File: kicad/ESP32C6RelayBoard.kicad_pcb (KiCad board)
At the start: 2 copper layers, 110.5 x 85.5 mm, 123 parts, among them IC1 SPX1117M3-L-3-3_TR, J1 Screw_Terminal_01x02, J10 Screw_Terminal_01x03, J11 Screw_Terminal_01x03, J12 Screw_Terminal_01x03, J13 Screw_Terminal_01x03, J2 Conn_02x08_Odd_Even, J3 Screw_Terminal_01x02, J4 Screw_Terminal_01x02, J5 10118192-0001LF, J6 Screw_Terminal_01x02, J7 Screw_Terminal_01x02, J8 Screw_Terminal_01x03, J9 Screw_Terminal_01x03, K1 G5RL-K1-E-DC12, K2 G5RL-K1-E-DC12, K3 G5RL-K1-E-DC12, K4 G5RL-K1-E-DC12, Q1 FDN302P, U1 AP62300Z6-7, U10 INA232AIDDFR, U11 74HC237, U12 INA232AIDDFR, U13 FAN3241TMX, U14 FAN3241TMX, U2 ESP32-C6-MINI-1/U, U3 434133025816, U4 434133025816, U5 ESD401DPYR, U6 ESD401DPYR, U7 ESD401DPYR, U8 FAN3241TMX, U9 FAN3241TMX

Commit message: Added LED
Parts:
- added D2: WS2812B, LED_SMD:LED_WS2812B_PLCC4_5.0x5.0mm_P3.2mm, F.Cu at (158.5, 86.8)
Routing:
- net /GPIO8: track 104.5 -> 151.8 mm, vias 1 -> 3
- net +3V3: track 205.2 -> 231.7 mm
- net GND: track 237.9 -> 239.6 mm, vias 92 -> 93
- net /CHIP_PU: track 156.9 -> 158.3 mm
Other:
- board text added: "1"
- board text added: "2"
- board text added: "3"
- board text added: "4"
- board text removed: "BOOT"
- board text removed: "RST"

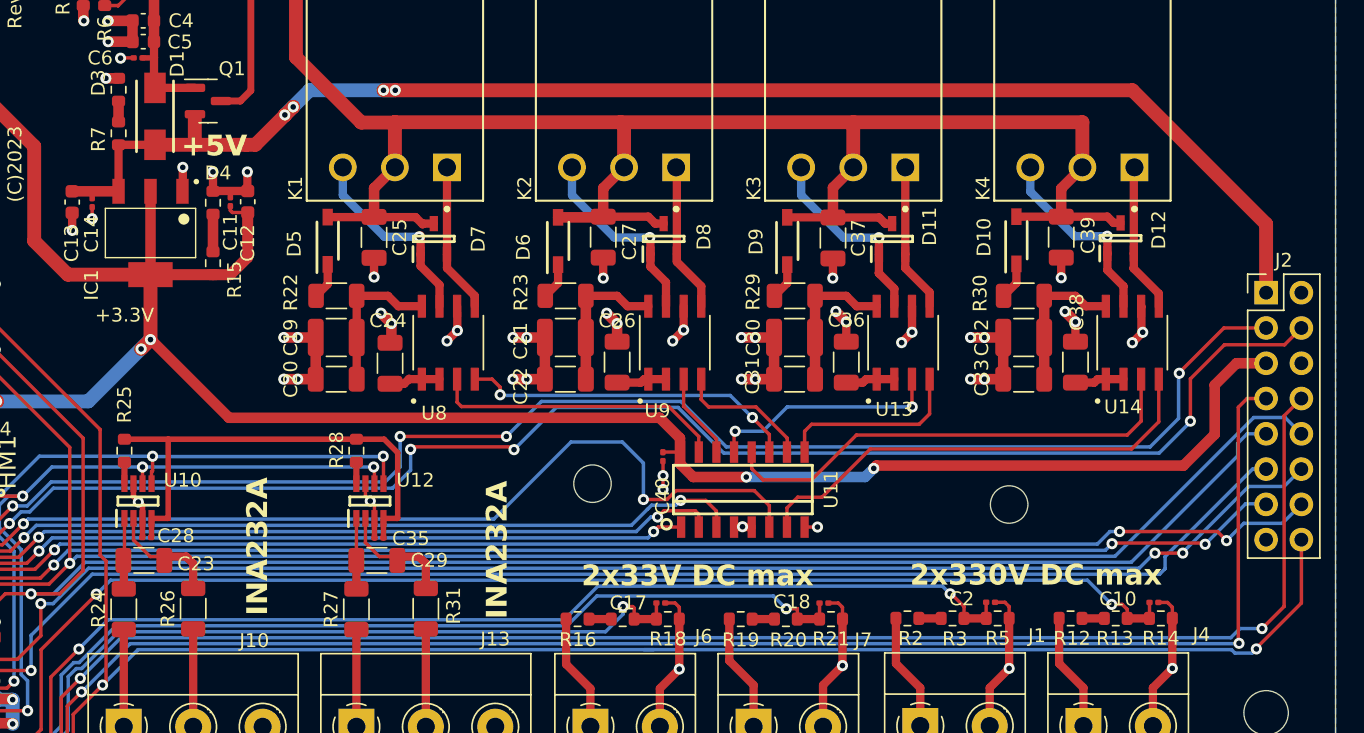
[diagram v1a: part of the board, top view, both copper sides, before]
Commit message: Added pin names to EXT connector. Generated schema in .pdf.
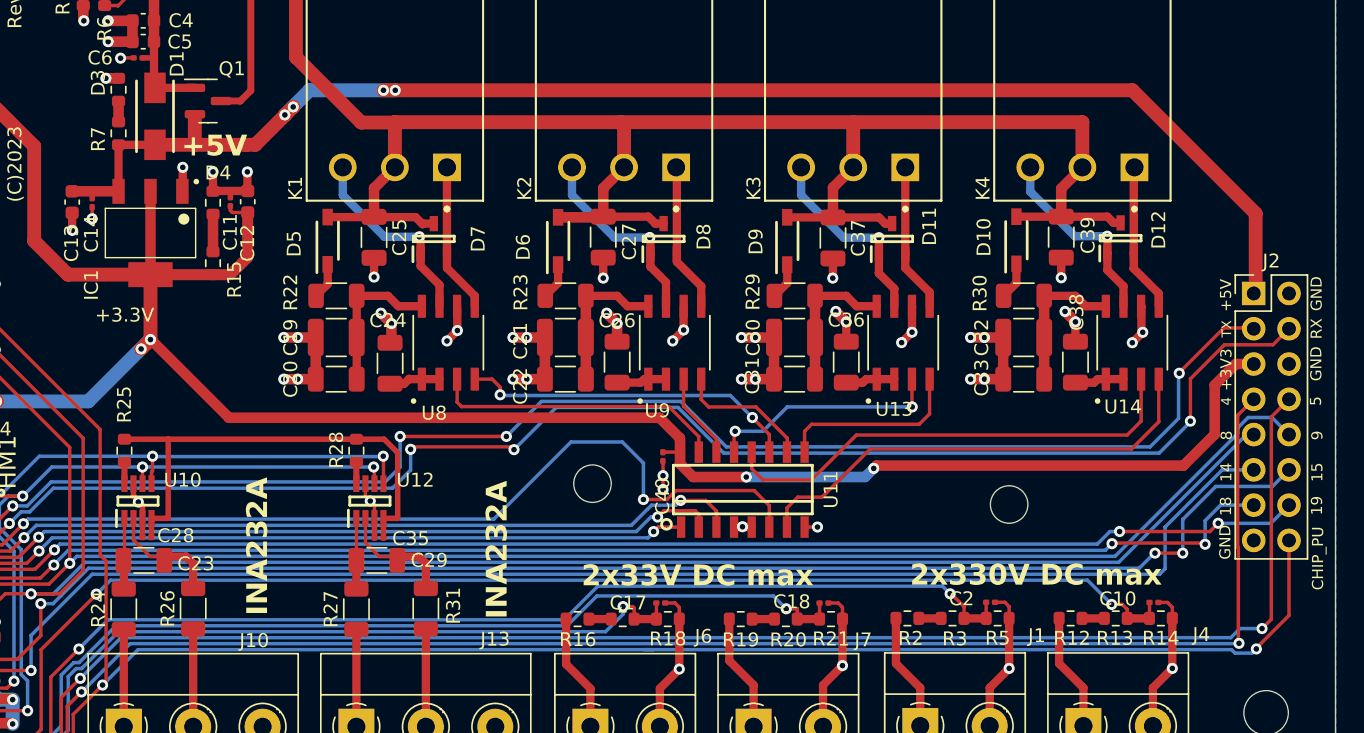
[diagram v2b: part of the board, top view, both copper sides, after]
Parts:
- moved J2 0.89 mm to (257.1, 103.8)
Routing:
- net /GPIO19: track 102.7 -> 101.3 mm
- net /GPIO8: track 151.8 -> 150.4 mm
- net /GPIO4: track 123.1 -> 121.9 mm
- net +3V3: track 231.7 -> 230.8 mm
- net /U0TXD: track 115.1 -> 114.2 mm
- net /U0RXD: track 116.5 -> 115.7 mm
- net /GPIO9: track 145.2 -> 144.5 mm
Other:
- board text added: "+3V3"
- board text added: "14"
- board text added: "15"
- board text added: "18"
- board text added: "19"
- board text added: "5"
- board text added: "8"
- board text added: "9"
- board text added: "CHIP_PU"
- board text added: "GND"
- board text added: "RX"
- board text added: "TX"

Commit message: Exposed also SCL and SDO on EXT connector
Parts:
- J2: value Conn_02x08_Odd_Even -> Conn_02x09_Odd_Even; footprint Connector_PinHeader_2.54mm:PinHeader_2x08_P2.54mm_Vertical -> Connector_PinHeader_2.54mm:PinHeader_2x09_P2.54mm_Vertical
- moved R28 0.42 mm to (192.1, 115.1)
- moved J2 0.06 mm to (257.1, 103.8)
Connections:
- J2 pad 15: GND -> /SCL
- J2 pad 16: /CHIP_PU -> /SDA
- U12 pad 7: GND -> +3.3V
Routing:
- net /SDA: track 56.8 -> 131.2 mm, vias 4 -> 6
- net /SCL: track 55.7 -> 126.6 mm, vias 4 -> 6
- net GND: track 239.6 -> 245.9 mm, vias 93 -> 101
- net /WR: track 74.0 -> 69.1 mm
- net +3.3V: track 35.5 -> 40.2 mm
- net /CHIP_PU: track 157.9 -> 155.6 mm
- net /GPIO9: track 144.5 -> 145.9 mm
- net /GPIO8: track 150.4 -> 151.4 mm
- net Net-(U12-ALERT): track 1.55 -> 2.11 mm
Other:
- board text added: "SCL"
- board text added: "SDA"

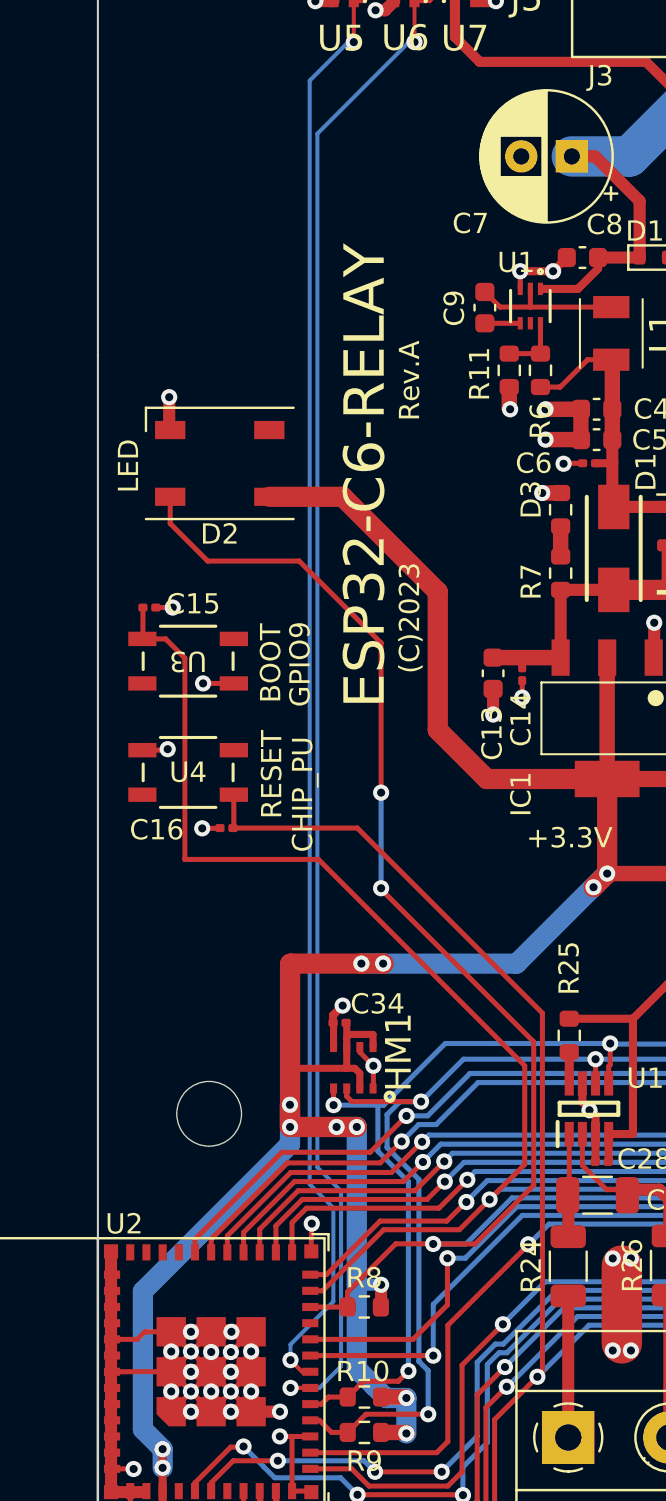
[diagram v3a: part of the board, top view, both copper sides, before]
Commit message: Moved buttons and LED away from CPU
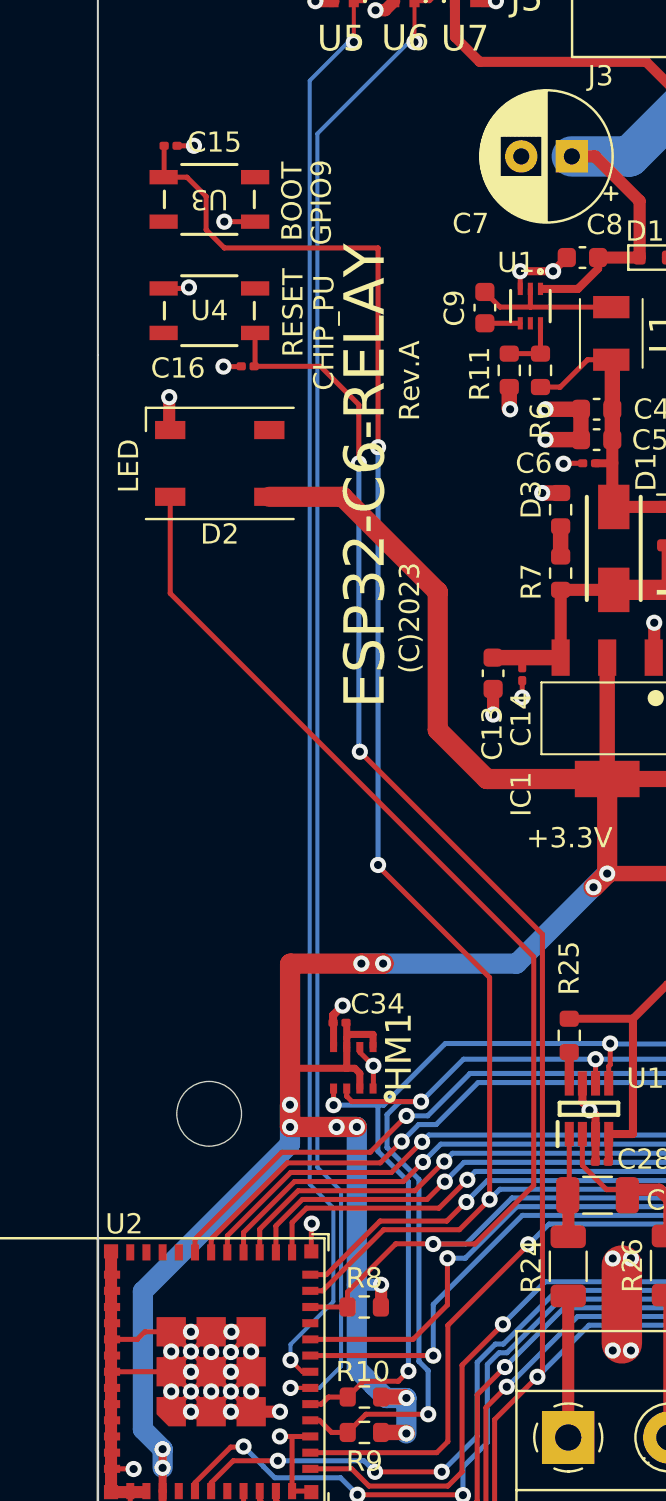
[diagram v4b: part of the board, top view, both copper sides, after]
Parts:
- moved C16 22.8 mm to (159.9, 82.0)
- moved U3 22.8 mm to (158.0, 73.8)
- moved U4 22.8 mm to (158.0, 79.3)
- moved C15 22.8 mm to (156.1, 71.2)
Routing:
- net /GPIO9: track 145.9 -> 167.5 mm, vias 1 -> 3
- net /CHIP_PU: track 155.6 -> 176.5 mm, vias 2 -> 4
- net /GPIO8: track 151.4 -> 148.5 mm, vias 3 -> 1

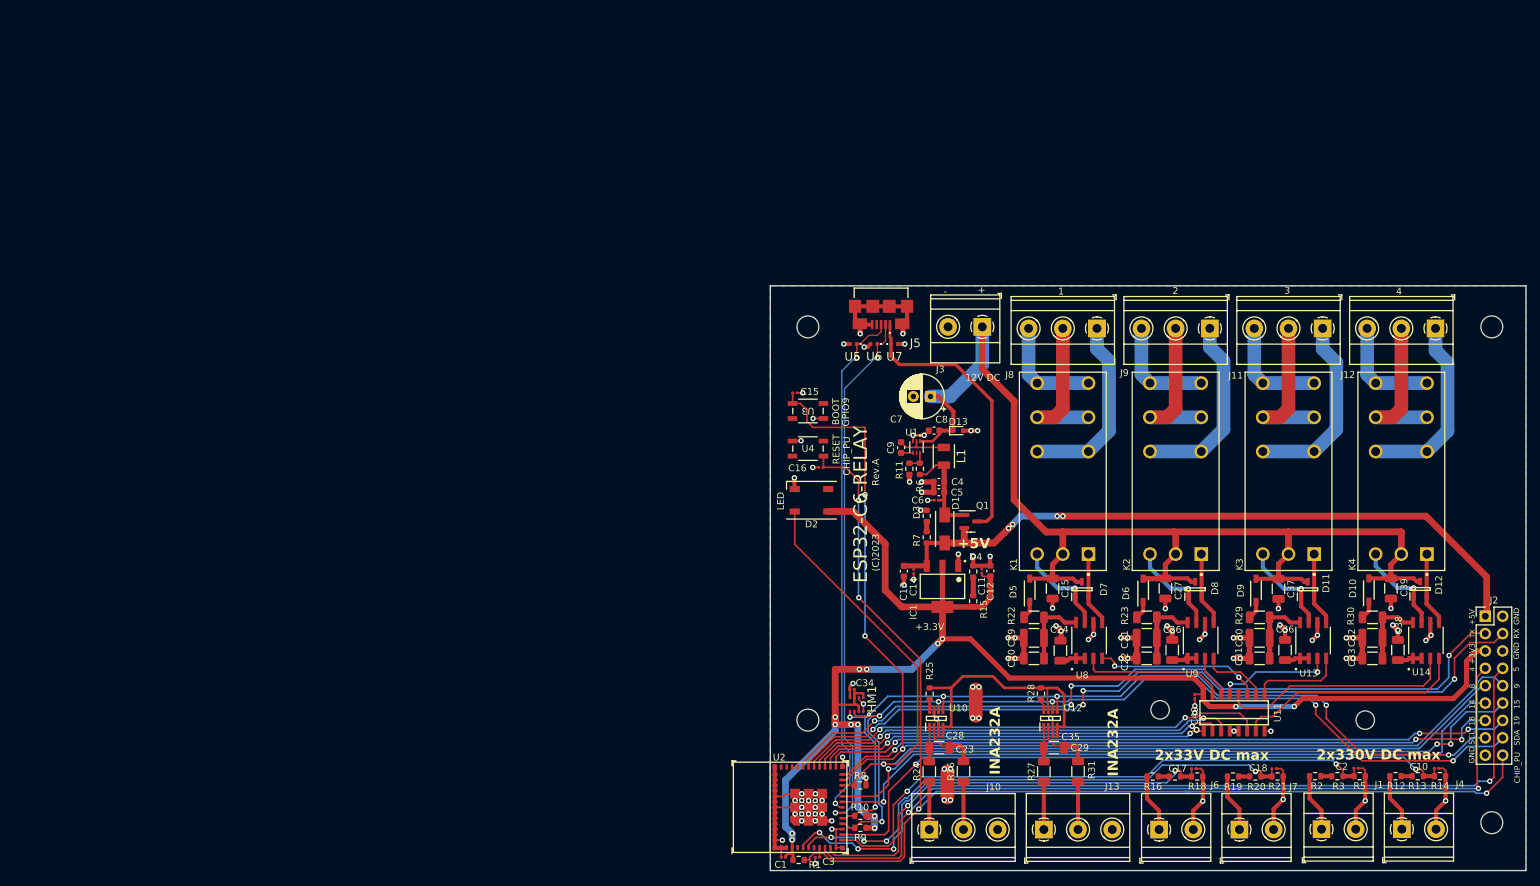
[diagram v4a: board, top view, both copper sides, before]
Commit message: Added 3D models to the project
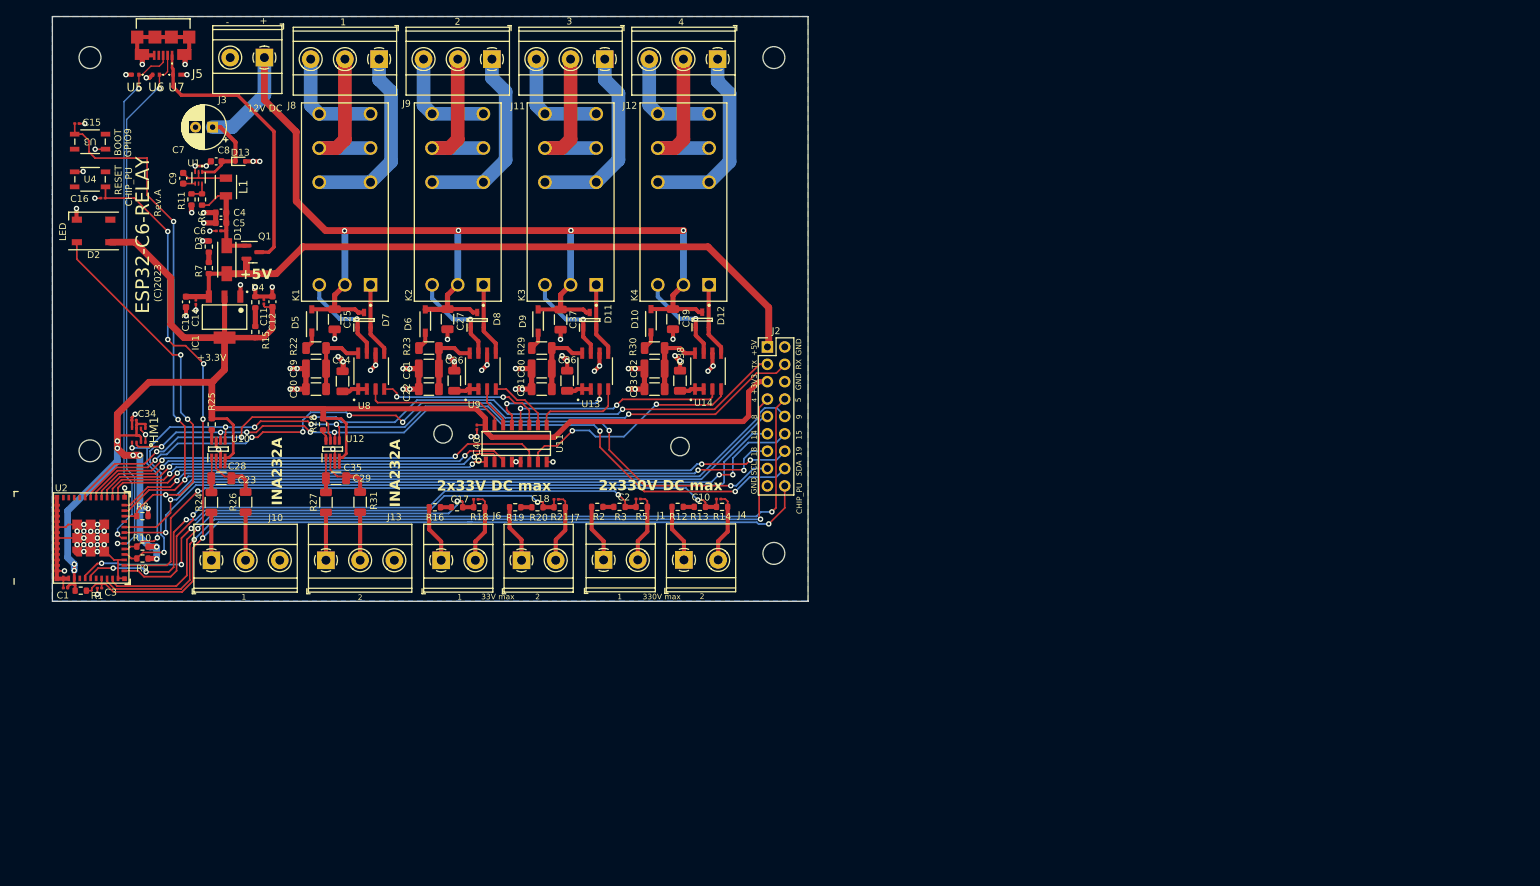
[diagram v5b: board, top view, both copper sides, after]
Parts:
- moved REF** 112.3 mm to (104.7, 77.2)
- moved D4 112.1 mm to (77.2, 57.9)
- moved D6 112.1 mm to (102.0, 60.6)
- moved D9 112.1 mm to (118.5, 60.6)
- moved C10 112.1 mm to (145.0, 86.7)
- moved C13 112.1 mm to (67.1, 57.8)
- moved C15 112.1 mm to (51.1, 31.8)
- moved C16 112.1 mm to (54.9, 42.7)
- moved C17 112.1 mm to (109.4, 86.7)
- moved C2 112.1 mm to (133.2, 86.7)
- moved C28 112.1 mm to (72.4, 82.0)
- moved C29 112.1 mm to (89.0, 83.7)
- moved C32 112.1 mm to (135.6, 67.6)
- moved C33 112.1 mm to (135.6, 70.6)
- moved C34 112.1 mm to (59.5, 75.1)
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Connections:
- C28 pad 1: +3.3V -> +3V3
- C35 pad 1: +3.3V -> +3V3
- R25 pad 2: +3.3V -> +3V3
- R28 pad 2: +3.3V -> +3V3
- U10 pad 4: +3.3V -> +3V3
- U12 pad 4: +3.3V -> +3V3
- U12 pad 7: +3.3V -> +3V3
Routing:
- net +3.3V: track 40.2 -> 0.00 mm
- net +3V3: track 230.8 -> 262.7 mm, vias 15 -> 9
- net +12V: track 174.6 -> 188.7 mm, vias 0 -> 4
- net GND: track 245.9 -> 238.5 mm, vias 101 -> 87
- net /U0TXD: track 114.2 -> 111.4 mm
- net /ADC2: track 69.1 -> 66.4 mm
- net /R2S: track 17.5 -> 19.9 mm
- net /R3S: track 34.3 -> 32.4 mm, vias 0 -> 2
- net /SCL: track 126.6 -> 128.4 mm, vias 6 -> 8
- net +5V: track 103.4 -> 101.7 mm, vias 4 -> 0
- net /SDA: track 131.2 -> 132.6 mm, vias 6 -> 8
- net /U0RXD: track 115.4 -> 114.2 mm, vias 4 -> 6
- net /CHIP_PU: track 176.5 -> 177.6 mm, vias 4 -> 6
- net /ADC3: track 77.9 -> 78.7 mm
- net /S/R: track 63.8 -> 63.0 mm
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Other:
- board text added: "330V max"
- board text added: "33V max"
